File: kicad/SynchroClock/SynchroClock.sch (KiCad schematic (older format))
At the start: 32 parts, among them J1 SERIAL0, J4 CLOCK, SW1 SW_Push, U1 TC1262-33VAB, U2 MCP1702-1502E/TO, U3 ESP-12E, U4 DS3231, U5 ATTINY85-20PU, U6 DRV8838

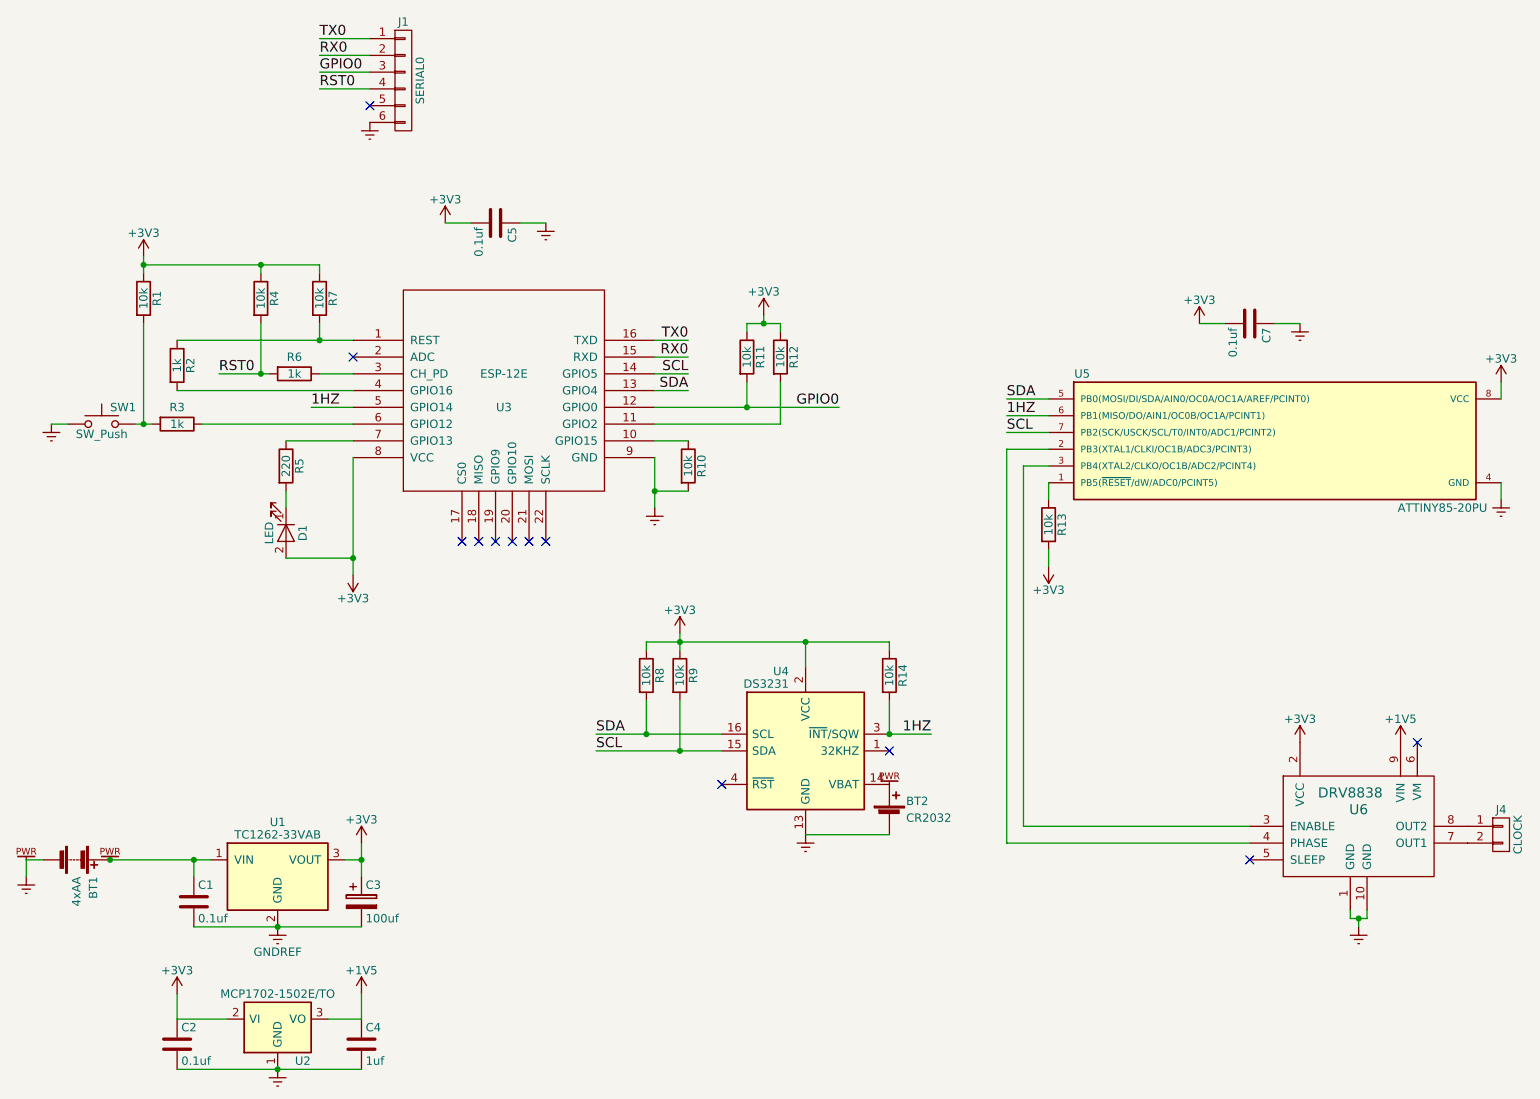
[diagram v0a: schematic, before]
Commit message: updated with reset & sleep changes
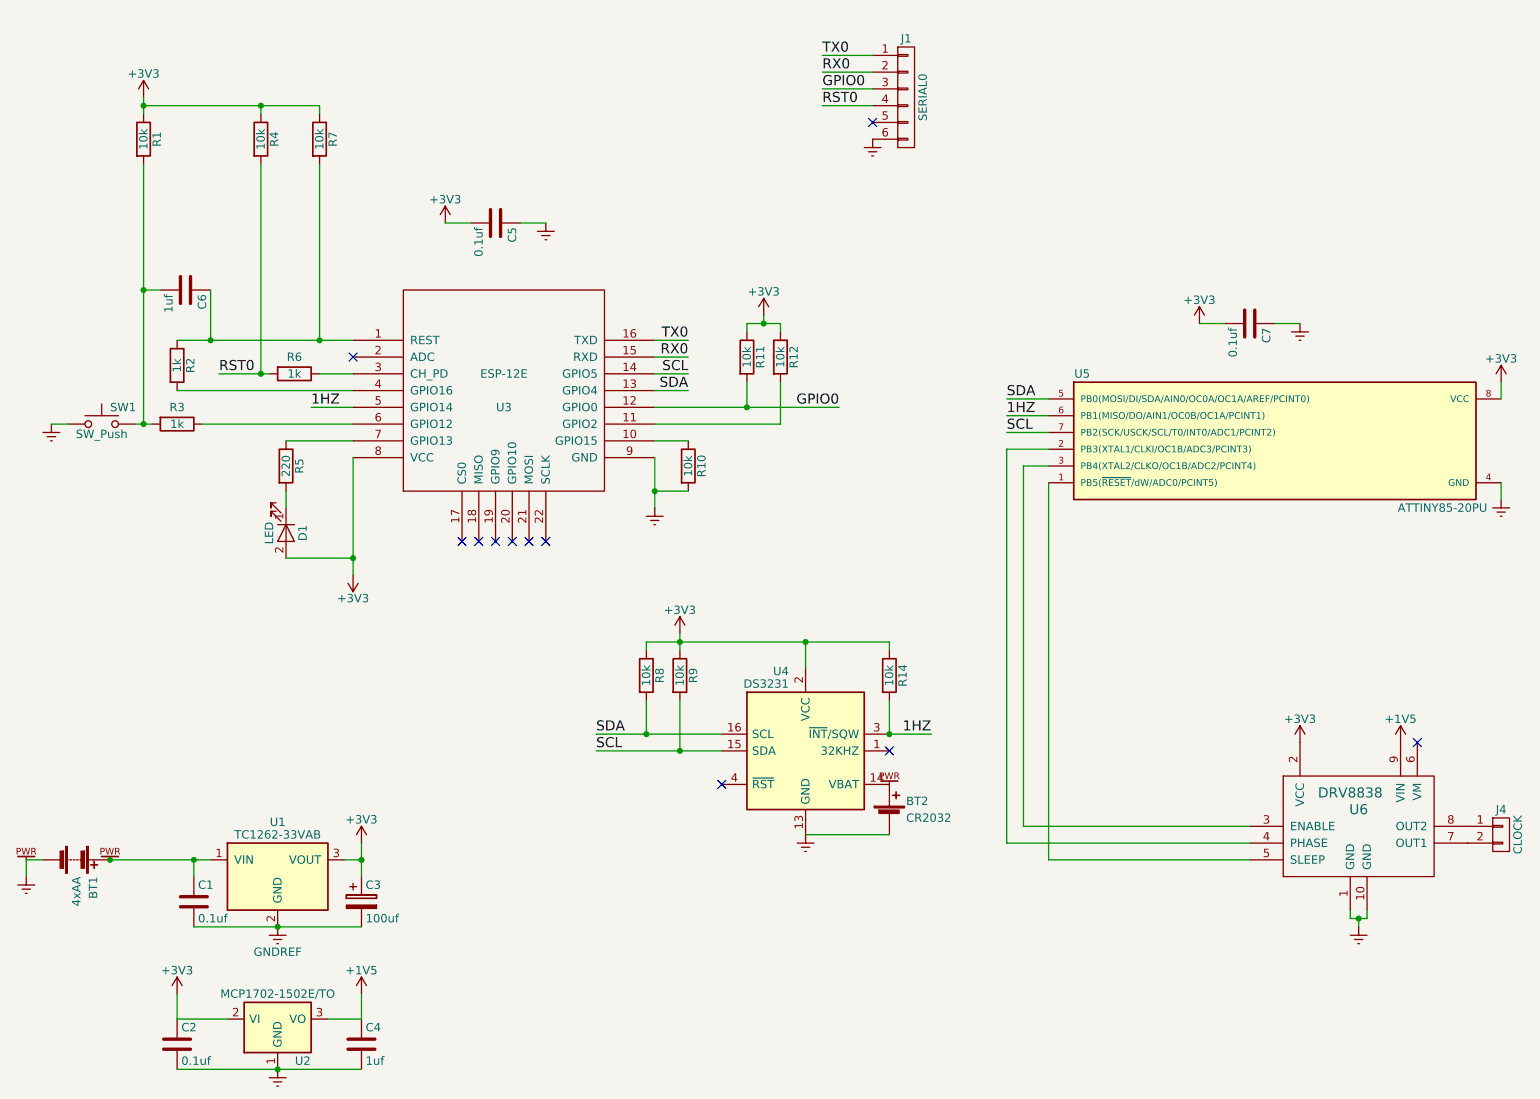
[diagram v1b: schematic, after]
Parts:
- removed R13: 10k, Resistors_THT:R_Axial_DIN0207_L6.3mm_D2.5mm_P2.54mm_Vertical, symbol R
- added C6: 1uf, Capacitors_THT:C_Disc_D5.0mm_W2.5mm_P2.50mm, symbol C
- J1: footprint Pin_Headers:Pin_Header_Straight_1x06_Pitch2.54mm -> Socket_Strips:Socket_Strip_Straight_1x05_Pitch2.54mm
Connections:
- net at R2.1, R7.2, U3.1 (REST): now also C6.1
- net at U6.5 (SLEEP): now also U5.1 (PB5(~RESET~/dW/ADC0/PCINT5))
- net at R1.2, R3.2, SW1.2: now also C6.2
- no-connect marks 12 -> 11
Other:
- moved on the sheet: J1, R1, R4, R7

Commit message: Version 0.2 of Board
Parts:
- BT1: footprint Pin_Headers:Pin_Header_Straight_1x02_Pitch2.54mm -> Connectors_JST:JST_XH_B02B-XH-A_02x2.50mm_Straight
- BT2: value CR2032 -> CR1220; footprint Connectors:CR2032V -> CR1220:CR1220-smd
- J1: footprint Socket_Strips:Socket_Strip_Straight_1x05_Pitch2.54mm -> Socket_Strips:Socket_Strip_Straight_1x06_Pitch2.54mm
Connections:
- net +1V5: now also U6.6 (VM); no longer U6.9 (VIN)
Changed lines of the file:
@@
 LIBS:contrib
 LIBS:valves
+LIBS:drv8838-pololu
+LIBS:ESP8266-12E
 LIBS:maxim
+LIBS:mcp1702
+LIBS:tc1262
 LIBS:switches
 LIBS:SynchroClock-cache
@@
 F 0 "BT1" H 1450 6150 50  0000 L CNN
 F 1 "4xAA" H 1450 6050 50  0000 L CNN
-F 2 "Pin_Headers:Pin_Header_Straight_1x02_Pitch2.54mm" V 1350 6110 50  0001 C CNN
+F 2 "Connectors_JST:JST_XH_B02B-XH-A_02x2.50mm_Straight" V 1350 6110 50  0001 C CNN
 F 3 "" V 1350 6110 50  0001 C CNN
 	1    1350 6050
@@
 L +1V5 #PWR09
 U 1 1 58FCEBFA
-P 9250 5350
-F 0 "#PWR09" H 9250 5200 50  0001 C CNN
-F 1 "+1V5" H 9250 5490 50  0000 C CNN
-F 2 "" H 9250 5350 50  0001 C CNN
-F 3 "" H 9250 5350 50  0001 C CNN
-	1    9250 5350
+P 9350 5350
+F 0 "#PWR09" H 9350 5200 50  0001 C CNN
+F 1 "+1V5" H 9350 5490 50  0000 C CNN
+F 2 "" H 9350 5350 50  0001 C CNN
+F 3 "" H 9350 5350 50  0001 C CNN
+	1    9350 5350
 	-1   0    0    -1
 $EndComp
@@
 P 6200 5800
 F 0 "BT2" H 6300 5900 50  0000 L CNN
-F 1 "CR2032" H 6300 5800 50  0000 L CNN
-F 2 "Connectors:CR2032V" V 6200 5860 50  0001 C CNN
+F 1 "CR1220" H 6300 5800 50  0000 L CNN
+F 2 "CR1220:CR1220-smd" V 6200 5860 50  0001 C CNN
 F 3 "" V 6200 5860 50  0001 C CNN
 	1    6200 5800
@@
 Text Label 5000 3050 2    60   ~ 0
 RX0
-NoConn ~ 9350 5350
 $Comp
 L CONN_01X02 J4
@@
 F 0 "J1" H 6300 1850 50  0000 C CNN
 F 1 "SERIAL0" V 6400 1500 50  0000 C CNN
-F 2 "Socket_Strips:Socket_Strip_Straight_1x05_Pitch2.54mm" H 6300 1500 50  0001 C CNN
+F 2 "Socket_Strips:Socket_Strip_Straight_1x06_Pitch2.54mm" H 6300 1500 50  0001 C CNN
 F 3 "" H 6300 1500 50  0001 C CNN
 	1    6300 1500
@@
 Wire Wire Line
 	7150 6050 8350 6050
+NoConn ~ 9250 5350
 $EndSCHEMATC
